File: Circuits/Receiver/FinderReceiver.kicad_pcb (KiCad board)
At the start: 2 copper layers, 61 x 38.1 mm, 8 parts, among them P1 WRITER, U1 TWE_LITE_SMD

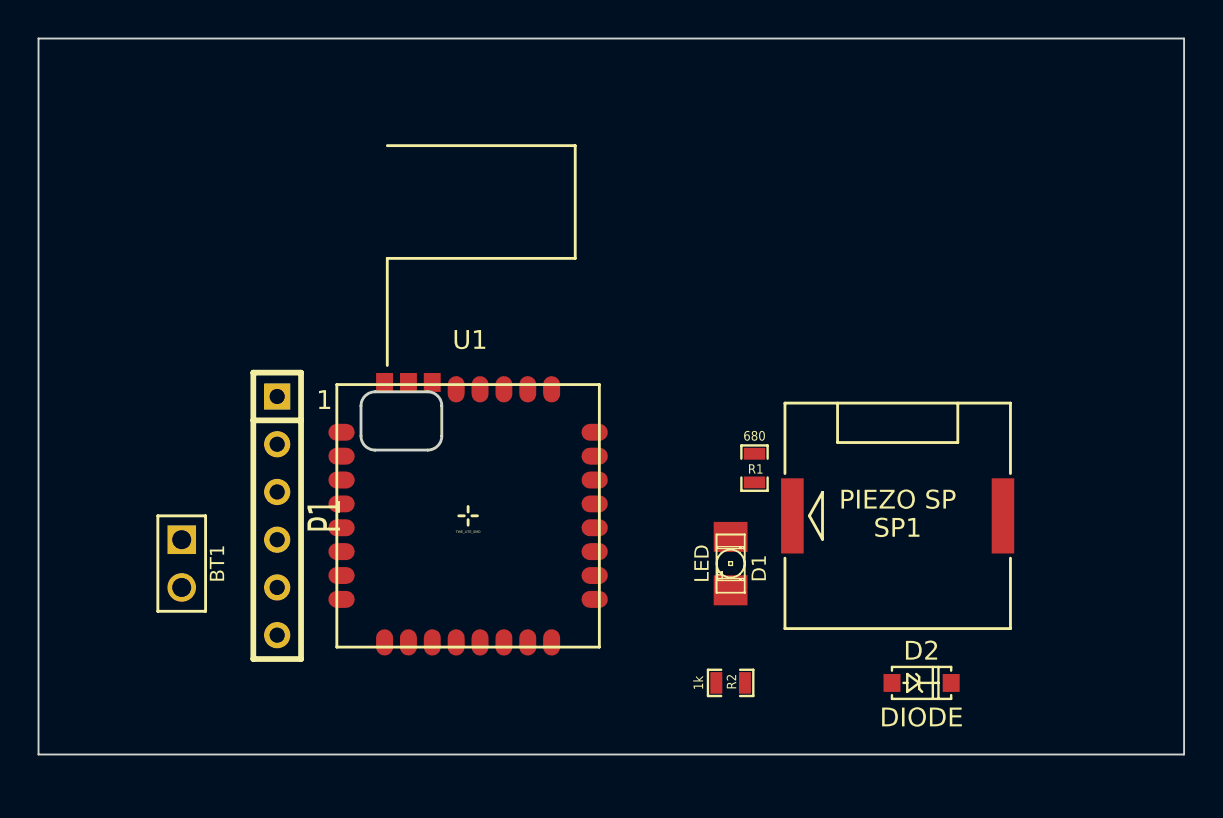
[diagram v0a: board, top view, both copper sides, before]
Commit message: Locate the TWE-Lite SMD on the front side.
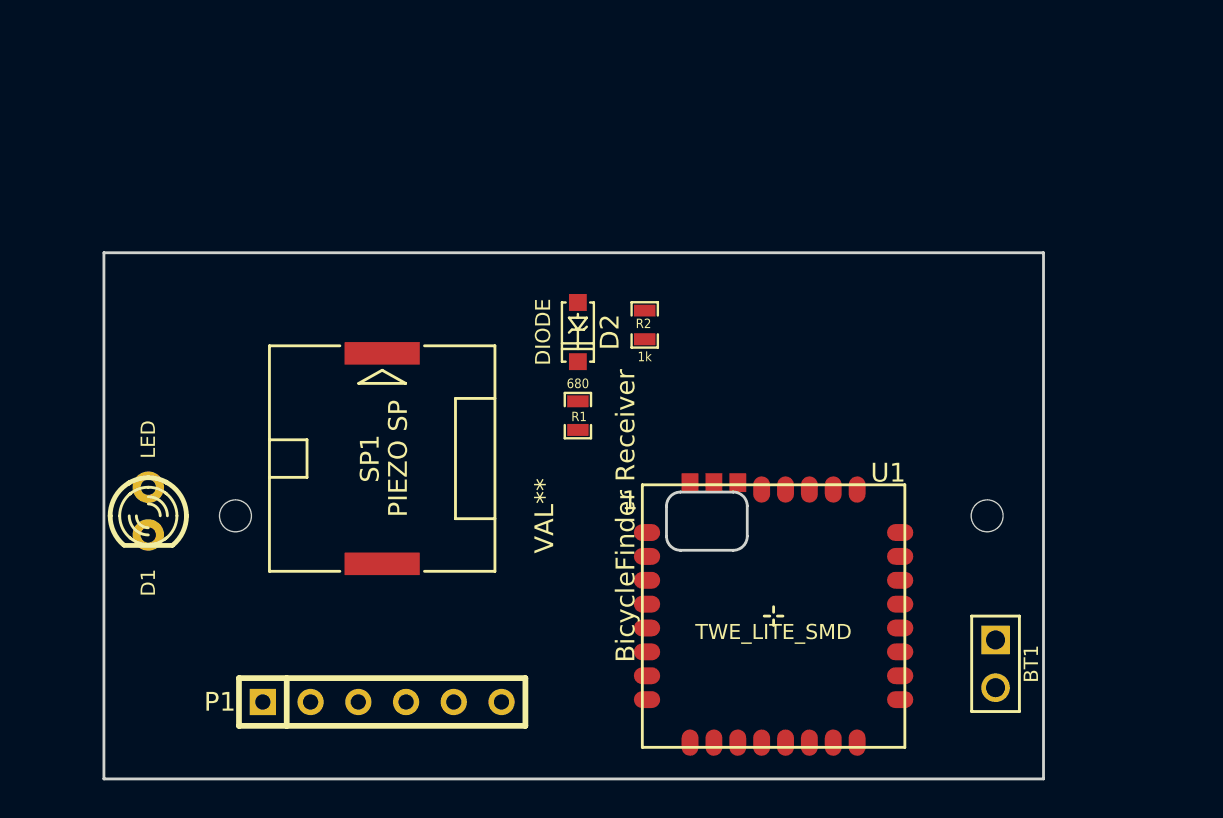
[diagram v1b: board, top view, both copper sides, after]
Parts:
- added BicycleFinder Receiver: VAL**, FINDER_RECEIVER, F.Cu at (203.2, 137.2)
- D1: footprint LED-1206 -> LED-3MM
- moved BT1 43.6 mm to (223.6, 145.0)
- moved D1 31.1 mm to (178.6, 136.9)
- moved SP1 27.6 mm to (191.0, 134.1), turned to 90 degrees
- moved D2 26.1 mm to (201.4, 127.4), turned to 270 degrees
- moved R2 19.6 mm to (205.0, 127.0), turned to 90 degrees
- moved U1 17.1 mm to (211.8, 142.5)
- moved P1 11.4 mm to (191.0, 147.1), turned to 0 degrees
- moved R1 9.80 mm to (201.4, 131.8)
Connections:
- D1 pad 1: N-0000030 -> /LED
- D1 pad 2: /LED -> /DO4
- R1 pad 2: N-0000030 -> /LED
- U1 pad 11: /LED -> /DO4
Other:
- board size 61 x 38.1 mm -> 50 x 28 mm
- net class Power added: clearance 0.254, trace_width 0.508, via_dia 0.889, via_drill 0.635

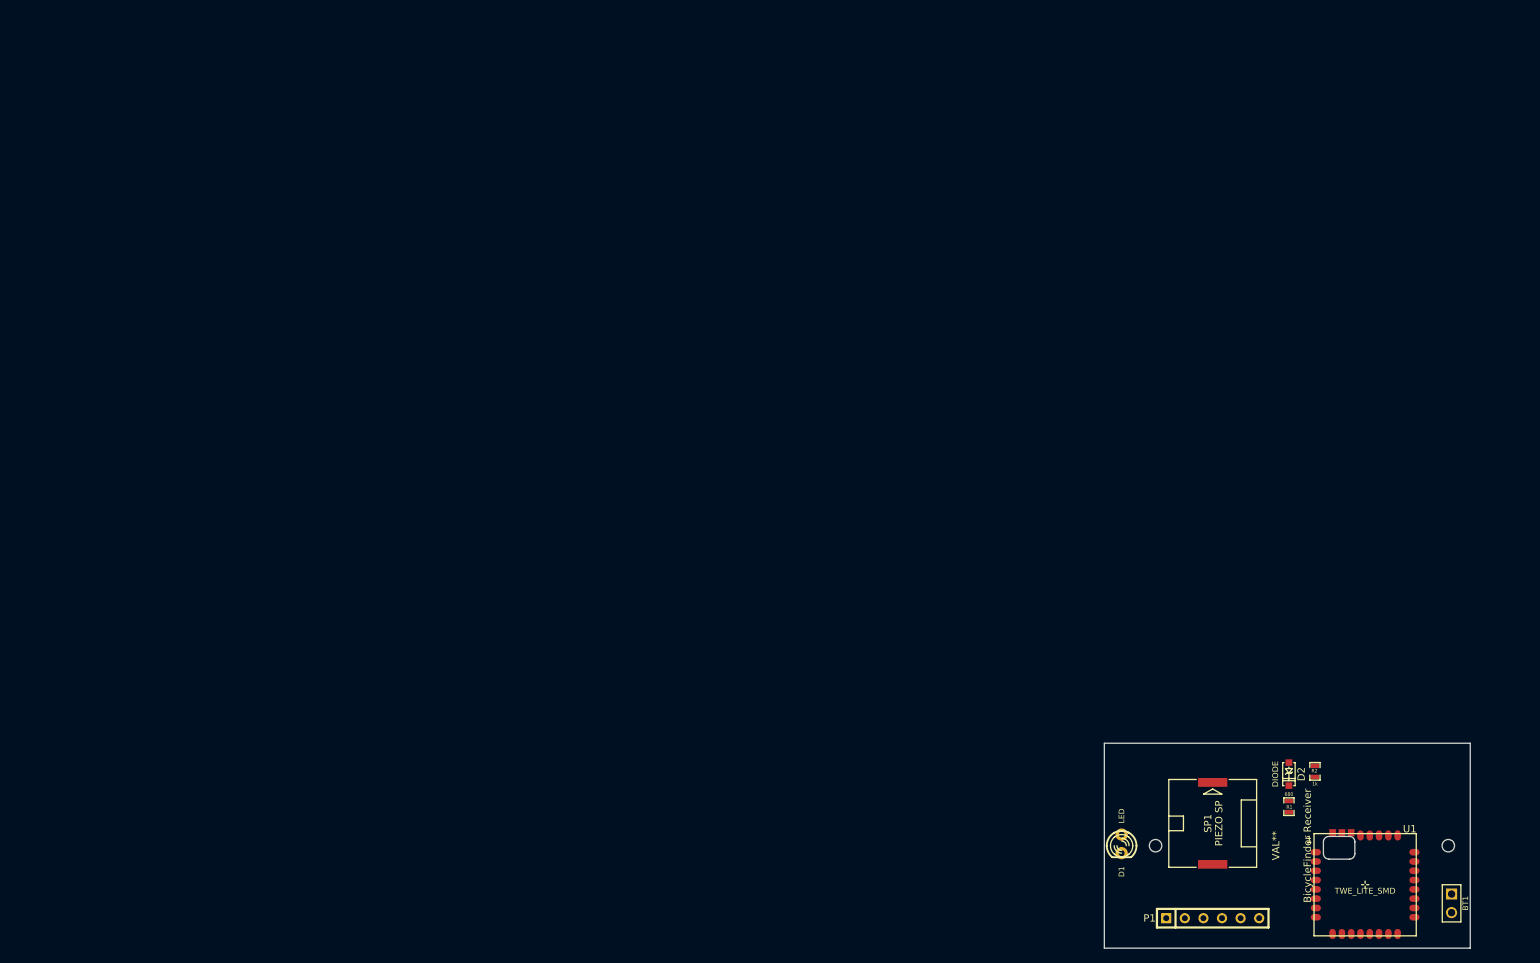
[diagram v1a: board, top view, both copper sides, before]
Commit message: Added spare footprints.
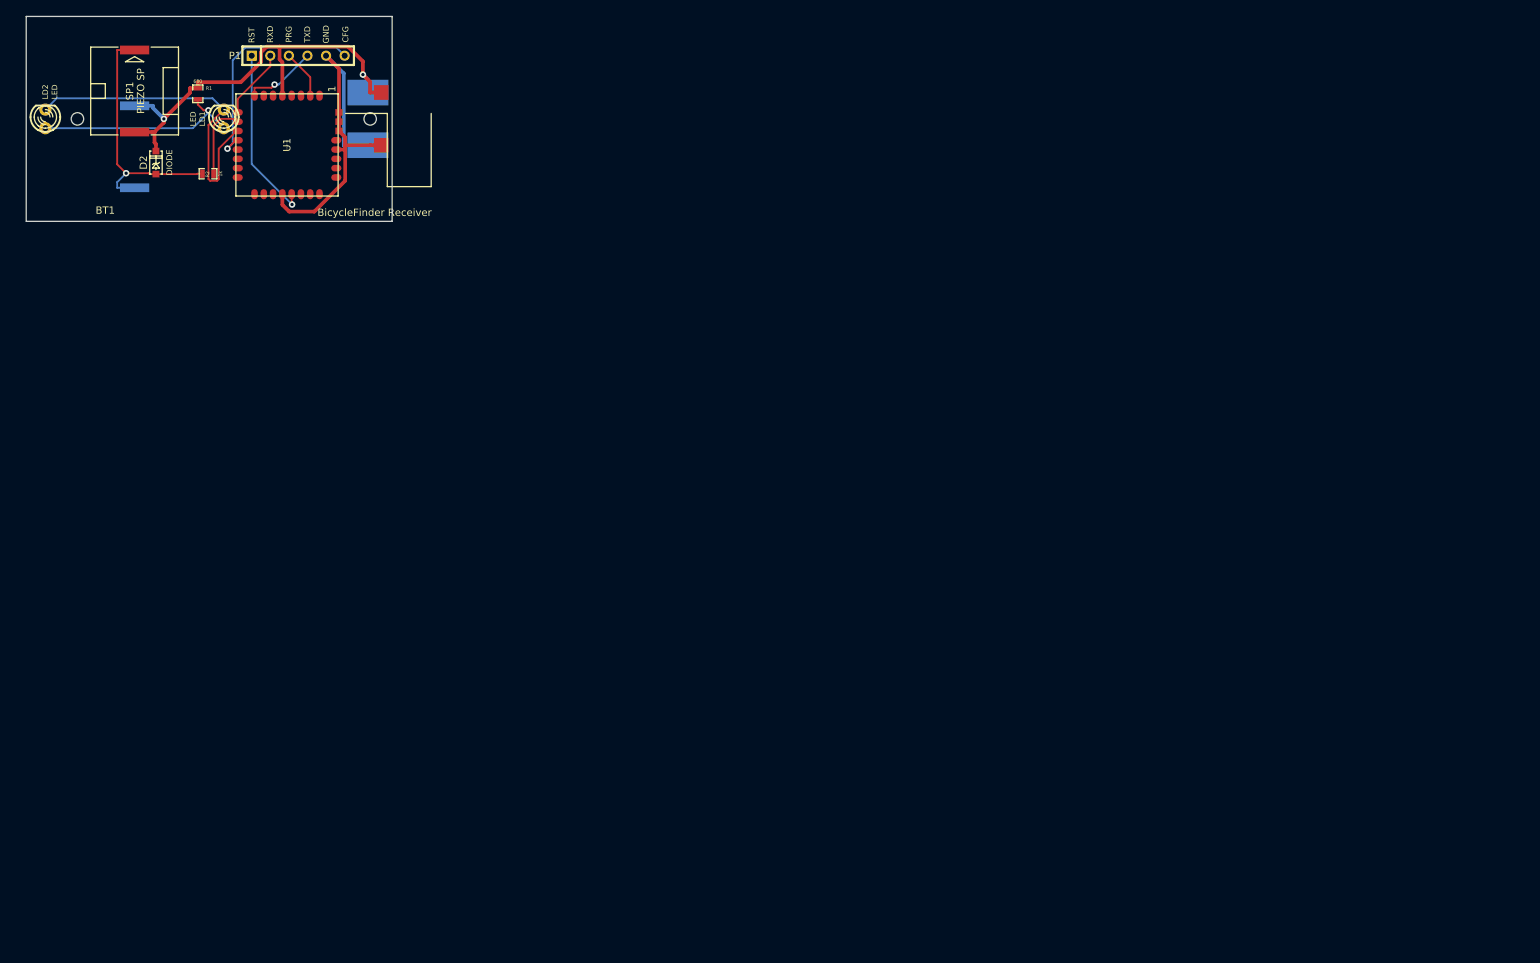
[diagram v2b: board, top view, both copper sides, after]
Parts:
- removed BicycleFinder Receiver: VAL**, FINDER_RECEIVER
- removed D1: LED, LED-3MM
- added LD1: LED, LED-3MM, F.Cu at (55.9, 37.8)
- added LD2: LED, LED-3MM, F.Cu at (31.5, 37.8)
- added SP2: PIEZO SP, PIEZOSPK, B.Cu at (43.7, 41.7)
- BT1: value BATTERY -> BicycleFinder Receiver; footprint PIN_ARRAY_2X1 -> FINDER_RECEIVER
- U1: footprint TWE-001L-SMD -> TWE-001L-SMD-noNTH
- moved BT1 199.1 mm to (55.9, 37.8), turned to 0 degrees
- moved U1 178.7 mm to (64.5, 41.4), turned to 270 degrees
- moved R1 178.1 mm to (52.3, 34.4)
- moved SP1 178.1 mm to (43.7, 34.0)
- moved D2 175.9 mm to (46.6, 43.8), turned to 90 degrees
- moved R2 171.9 mm to (53.7, 45.3), turned to 180 degrees
- moved P1 171.8 mm to (66.0, 29.2)
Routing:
- net VCC: track 0.00 -> 62.2 mm, vias 0 -> 2
- net GND: track 0.00 -> 53.0 mm
- net /DO4: track 0.00 -> 45.4 mm
- net /SPK: track 0.00 -> 35.1 mm, vias 0 -> 1
- net /CFG: track 0.00 -> 30.7 mm, vias 0 -> 1
- net /LED: track 0.00 -> 28.9 mm, vias 0 -> 1
- net /RST: track 0.00 -> 24.1 mm, vias 0 -> 1
- net /SOUND: track 0.00 -> 10.4 mm
- net /TXD: track 0.00 -> 10.1 mm, vias 0 -> 1
- net /RXD: track 0.00 -> 9.59 mm
- net /PRG: track 0.00 -> 6.67 mm
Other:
- board text added: "CFG"
- board text added: "GND"
- board text added: "PRG"
- board text added: "RST"
- board text added: "RXD"
- board text added: "TXD"

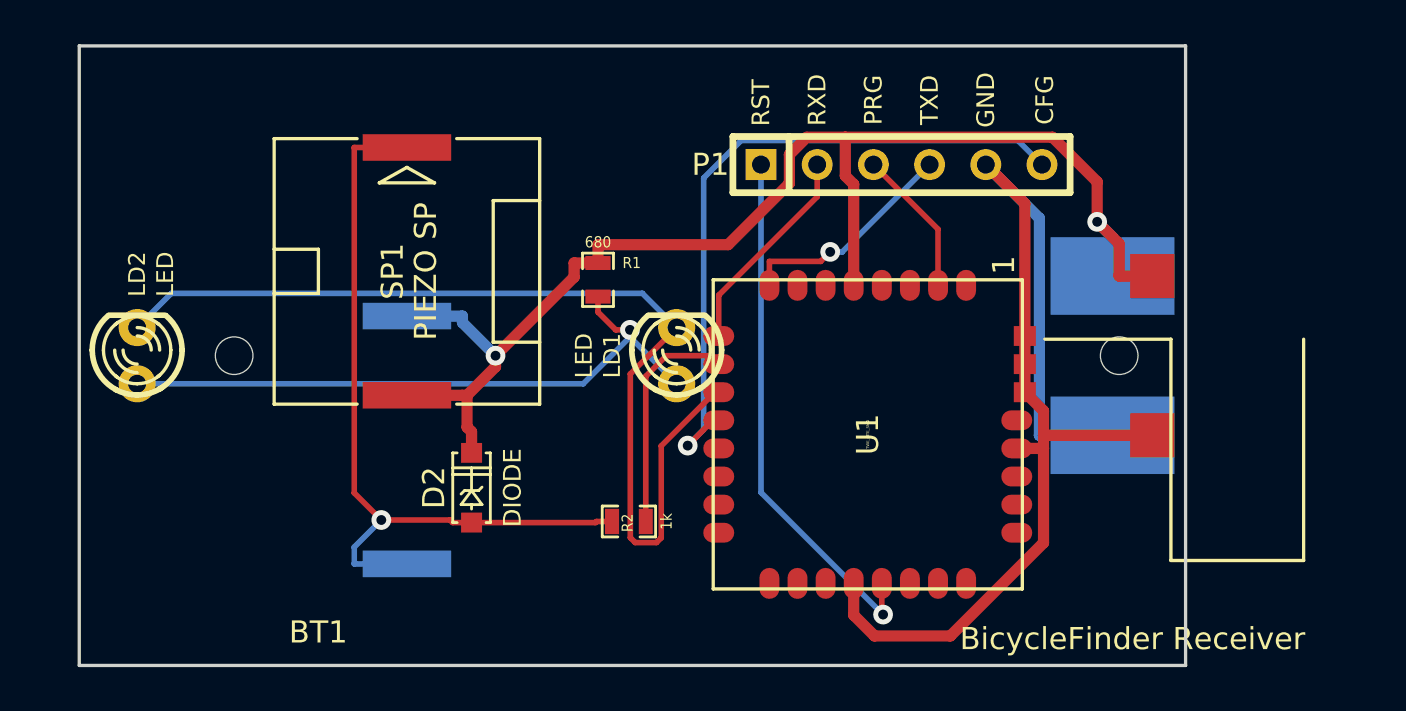
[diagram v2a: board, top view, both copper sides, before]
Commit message: Fixed: LED location.
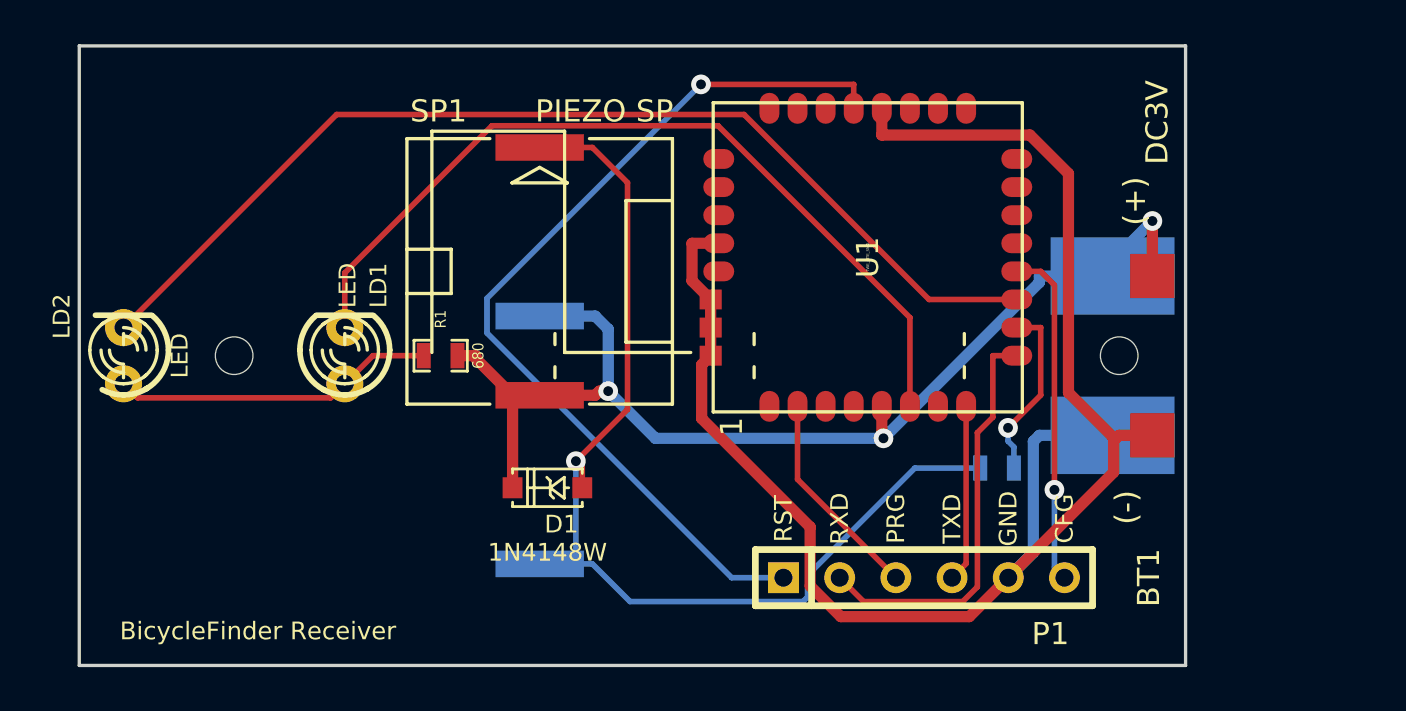
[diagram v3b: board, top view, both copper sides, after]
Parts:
- removed D2: DIODE, SOD123
- added D1: 1N4148W, SOD123, F.Cu at (50.0, 43.8)
- BT1: value BicycleFinder Receiver -> DC3V
- P1: footprint SIL-6 -> WRITER-6P
- R2: moved to B.Cu
- moved P1 18.7 mm to (65.8, 47.9)
- moved R2 16.8 mm to (70.4, 42.9)
- moved LD1 15.0 mm to (40.9, 37.8)
- moved U1 8.00 mm to (64.5, 33.4), turned to 90 degrees
- moved R1 7.90 mm to (45.2, 37.8), turned to 180 degrees
- moved SP1 6.00 mm to (49.7, 34.0)
- moved SP2 6.00 mm to (49.7, 41.7)
- moved LD2 0.62 mm to (30.9, 37.8)
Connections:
- LD1 pad 2: /DO4 -> /DO3
- U1 pad 6: (no net) -> /DO3
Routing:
- net /DO3: track 0.00 -> 38.4 mm
- net GND: track 53.0 -> 73.1 mm
- net /RST: track 24.1 -> 41.2 mm
- net /CFG: track 30.7 -> 15.4 mm
- net /LED: track 28.9 -> 14.6 mm, vias 1 -> 0
- net /SPK: track 35.1 -> 48.0 mm
- net VCC: track 62.2 -> 52.1 mm, vias 2 -> 3
- net /RXD: track 9.59 -> 18.8 mm
- net /PRG: track 6.67 -> 9.58 mm
- net /DO4: track 45.4 -> 47.8 mm
- net /SOUND: track 10.4 -> 8.15 mm, vias 0 -> 1
- net /TXD: track 10.1 -> 8.01 mm, vias 1 -> 0
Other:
- board text added: "(+)"
- board text added: "(-)"
- board text added: "BicycleFinder Receiver"
- board text removed: "CFG"
- board text removed: "GND"
- board text removed: "PRG"
- board text removed: "RST"
- board text removed: "RXD"
- board text removed: "TXD"
